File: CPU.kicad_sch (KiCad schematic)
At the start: 14 parts, among them J8 ISP, U4 STM32F405RGTx, Y1 8MHz

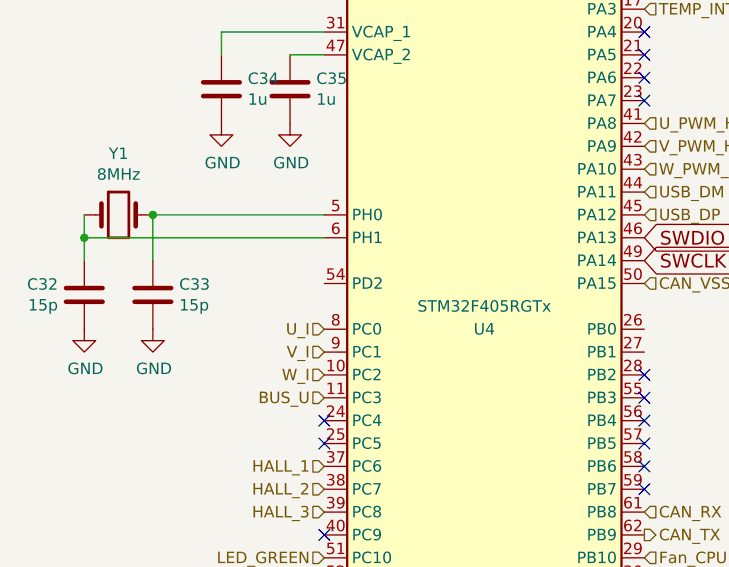
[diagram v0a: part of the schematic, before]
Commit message: - peeled back the filler planes around HV logic - improved insulation on HV logic
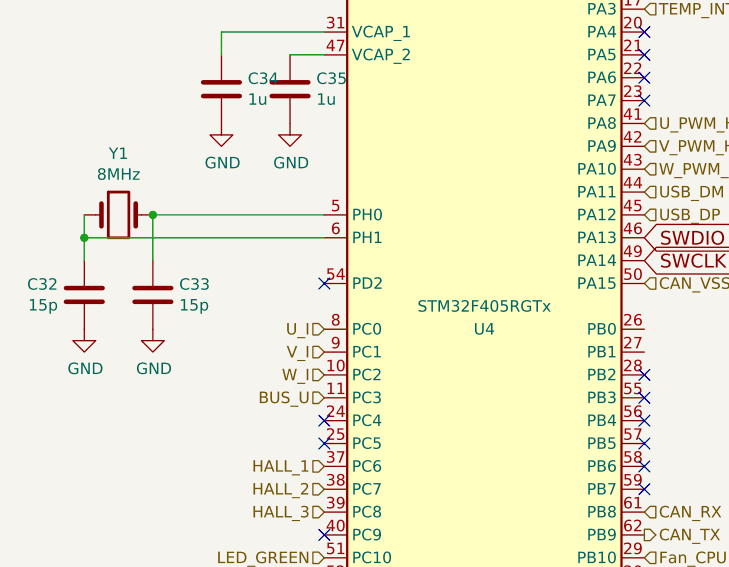
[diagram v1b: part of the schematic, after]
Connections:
- no-connect marks 18 -> 19
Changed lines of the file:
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@@
   )
   (no_connect (at 127 106.68))
+  (no_connect (at 127 88.9))
   (no_connect (at 162.56 101.6))
   (no_connect (at 127 129.54))

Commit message: - fixed some bugs
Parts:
- removed C40: 1u, Capacitor_SMD:C_0805_2012Metric, symbol Device:C
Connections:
- net NRST is gone; now on net +3V3: U4.7 (NRST)
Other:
- note removed: "Reset pin internally pulled up"
- moved on the sheet: C41
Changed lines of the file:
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@@
   (junction (at 251.46 25.4) (diameter 0) (color 0 0 0 0)
   )
-  (junction (at 257.81 25.4) (diameter 0) (color 0 0 0 0)
-  )
   (junction (at 238.76 25.4) (diameter 0) (color 0 0 0 0)
   )
@@
   (junction (at 245.11 38.1) (diameter 0) (color 0 0 0 0)
   )
-  (junction (at 257.81 38.1) (diameter 0) (color 0 0 0 0)
-  )
   (junction (at 107.95 81.28) (diameter 0) (color 0 0 0 0)
   )
@@
     (stroke (width 0) (type default))
   )
-  (wire (pts (xy 264.16 38.1) (xy 264.16 35.56))
-    (stroke (width 0) (type default))
-  )
   (wire (pts (xy 231.14 38.1) (xy 238.76 38.1))
     (stroke (width 0) (type default))
@@
     (stroke (width 0) (type default))
   )
-  (wire (pts (xy 264.16 25.4) (xy 264.16 27.94))
-    (stroke (width 0) (type default))
-  )
   (wire (pts (xy 127 81.28) (xy 107.95 81.28))
     (stroke (width 0) (type default))
@@
     (stroke (width 0) (type default))
   )
-  (wire (pts (xy 257.81 25.4) (xy 264.16 25.4))
-    (stroke (width 0) (type default))
-  )
   (wire (pts (xy 245.11 38.1) (xy 251.46 38.1))
     (stroke (width 0) (type default))
@@
     (stroke (width 0) (type default))
   )
-  (wire (pts (xy 257.81 38.1) (xy 264.16 38.1))
-    (stroke (width 0) (type default))
-  )
   (polyline (pts (xy 234.95 67.31) (xy 234.95 90.17))
     (stroke (width 0) (type default))
@@
     )
   )
-  (text "Reset pin internally\npulled up" (at 125.73 46.99 0)
-    (effects (font (size 1.016 1.016)) (justify right bottom))
-  )
   (text "Bypass, place next to VDD pins" (at 237.49 40.64 0)
     (effects (font (size 1.016 1.016)) (justify left bottom))
@@
     )
   )
-  (global_label "NRST" (shape input) (at 127 50.8 180)
-    (effects (font (size 1.524 1.524)) (justify right))
-    (property "Intersheetrefs" "${INTERSHEET_REFS}" (at 127 50.8 0)
-      (effects (font (size 1.27 1.27)) hide)
-    )
-  )
   (global_label "SWCLK" (shape input) (at 162.56 86.36 0)
     (effects (font (size 1.524 1.524)) (justify left))
@@
   (symbol (lib_id "Device:C") (at 257.81 31.75 0) (unit 1)
     (in_bom yes) (on_board yes) (dnp no)
-    (property "Reference" "C40" (at 259.08 29.21 0)
+    (property "Reference" "C41" (at 259.08 29.21 0)
       (effects (font (size 1.27 1.27)) (justify left))
     )
@@
       (project "HSWR"
         (path "/51094070-255e-40e7-bed5-d199e288e5dd/00000000-0000-0000-0000-00005899e230"
-          (reference "C40") (unit 1)
-        )
-      )
-    )
-  )
-  (symbol (lib_id "Device:C") (at 264.16 31.75 0) (unit 1)
-    (in_bom yes) (on_board yes) (dnp no)
-    (property "Reference" "C41" (at 265.43 29.21 0)
-      (effects (font (size 1.27 1.27)) (justify left))
-    )
-    (property "Value" "1u" (at 265.43 34.29 0)
-      (effects (font (size 1.27 1.27)) (justify left))
-    )
-    (property "Footprint" "Capacitor_SMD:C_0805_2012Metric" (at 265.1252 35.56 0)
-      (effects (font (size 1.27 1.27)) hide)
-    )
-    (property "Datasheet" "~" (at 264.16 31.75 0)
-      (effects (font (size 1.27 1.27)) hide)
-    )
-    (pin "1")
-    (pin "2")
-    (instances
-      (project "HSWR"
-        (path "/51094070-255e-40e7-bed5-d199e288e5dd/00000000-0000-0000-0000-00005899e230"
           (reference "C41") (unit 1)
         )
@@
         )
       )
+    )
+  )
+  (symbol (lib_id "power:+3V3") (at 127 50.8 0) (unit 1)
+    (in_bom yes) (on_board yes) (dnp no)
+    (property "Reference" "#PWR010" (at 127 54.61 0)
+      (effects (font (size 1.27 1.27)) hide)
+    )
+    (property "Value" "+3V3" (at 127.381 46.4058 0)
+      (effects (font (size 1.27 1.27)))
+    )
+    (property "Footprint" "" (at 127 50.8 0)
+      (effects (font (size 1.27 1.27)) hide)
+    )
+    (property "Datasheet" "" (at 127 50.8 0)
+      (effects (font (size 1.27 1.27)) hide)
+    )
+    (pin "1")
+    (instances
+      (project "HSWR"
+        (path "/51094070-255e-40e7-bed5-d199e288e5dd/00000000-0000-0000-0000-00005899e230"
+          (reference "#PWR010") (unit 1)
+        )
+      )
